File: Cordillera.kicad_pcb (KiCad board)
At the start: 2 copper layers, 337.2 x 122.6 mm, 209 parts, among them J1 Conn_01x08, Q1 2N7002, Q2 2N7002, SW1 SW_SPST, U1 STM32F072CBTx, U2 XC6206P332MR, U3 SRV05-4

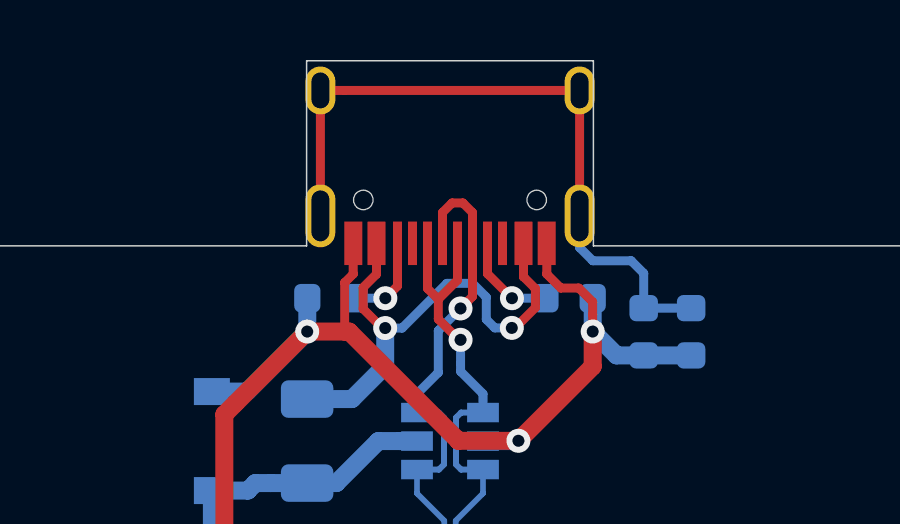
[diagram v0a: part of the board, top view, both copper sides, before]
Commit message: Switch to bottom-mount USB-C.
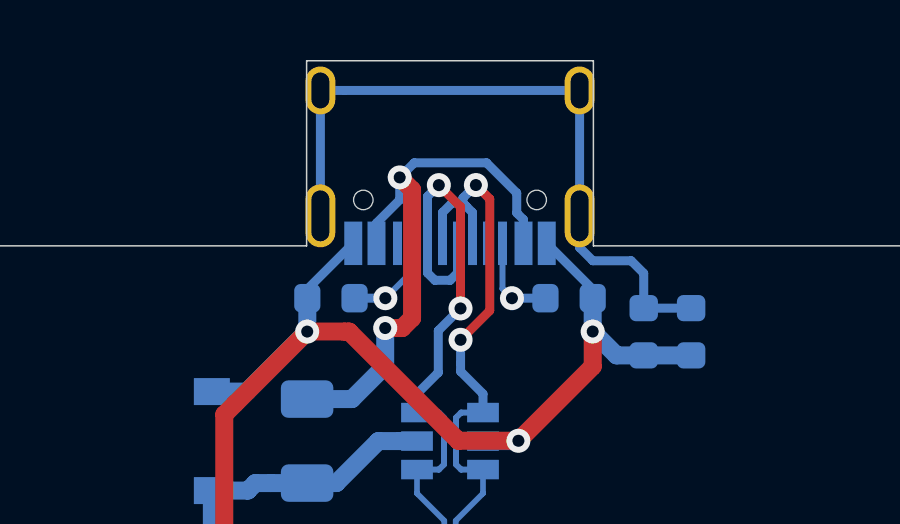
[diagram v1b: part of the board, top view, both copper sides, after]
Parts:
- USB1: moved to B.Cu
- turned USB1 to 0 degrees
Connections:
- USB1 pad 10: Net-(R3-Pad2) -> Net-(R2-Pad1)
- USB1 pad 4: Net-(R2-Pad1) -> Net-(R3-Pad2)
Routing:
- net /D-: track 59.3 -> 63.4 mm, vias 1 -> 2
- net /D+: track 59.2 -> 62.5 mm, vias 1 -> 2
- net GND: track 202.0 -> 199.9 mm
- net VBUS: track 17.1 -> 19.1 mm
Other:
- rule pad_to_mask_clearance: 0.05 -> 0
